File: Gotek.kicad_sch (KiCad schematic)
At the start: 72 parts, among them J10 Conn_01x04_Pin, J3 Conn_01x03_Pin, J4 Conn_01x02_Pin, J7 Display Port, P1 Conn_01x26, P3 USB_A, Q1 PMBT2222A,215, Q2 PMBT2222A,215, Q3 PMBT2222A,215, Q4 PMBT2222A,215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

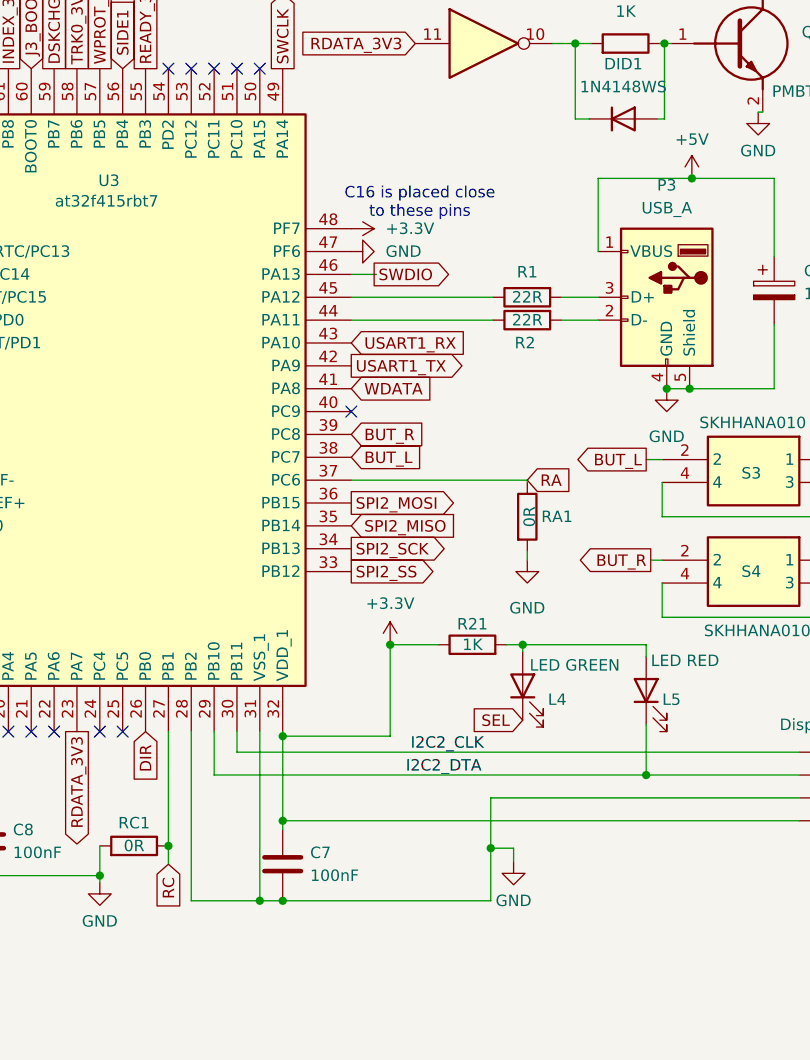
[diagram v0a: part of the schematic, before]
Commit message: Add files via upload
Updated to correct schematic positioning of C7 and C16. Layout did not change.
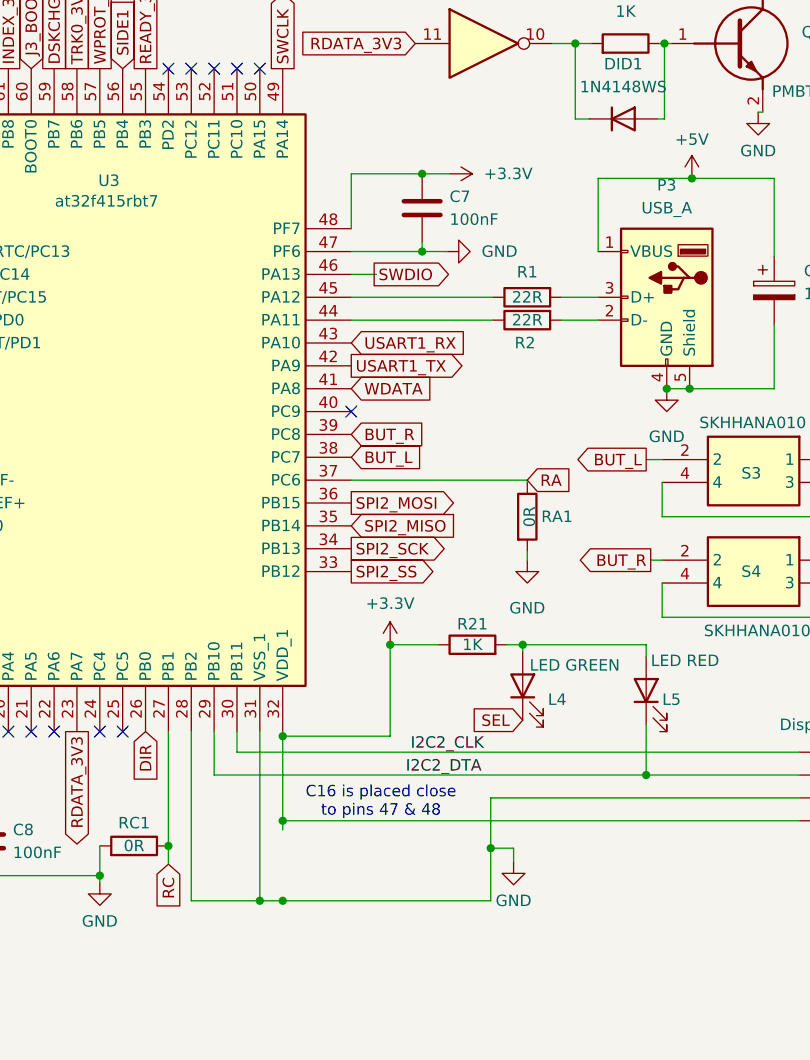
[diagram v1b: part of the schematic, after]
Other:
- note added: "C16 is placed close to pins 47 & 48"
- note removed: "C16 is placed close to these pins"
- moved on the sheet: C7
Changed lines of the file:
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@@
 	(title_block
 		(title "Gotek SFR1M44-DU26 (SFRC2D.B) Handrawn Schematic")
-		(date "2024-10-06")
+		(date "2024-10-09")
 		(rev "1.0")
 		(company "LiveBoxAndy")
 		(comment 1 "Based on pictures and meter readings.")
+		(comment 2 "Correct positions of C7 and C16 on schematic. Layout was correct")
 	)
 	(junction
@@
 	)
 	(junction
+		(at 231.394 92.456)
+		(diameter 0)
+		(color 0 0 0 0)
+	)
+	(junction
 		(at 280.416 33.274)
 		(diameter 0)
@@
 	)
 	(junction
+		(at 231.394 83.82)
+		(diameter 0)
+		(color 0 0 0 0)
+	)
+	(junction
 		(at 278.384 121.92)
 		(diameter 0)
@@
 	(wire
 		(pts
+			(xy 223.52 92.456) (xy 231.394 92.456)
+		)
+		(stroke
+			(width 0)
+			(type default)
+		)
+	)
+	(wire
+		(pts
 			(xy 227.838 136.144) (xy 233.172 136.144)
 		)
@@
 	(wire
 		(pts
+			(xy 231.394 92.456) (xy 234.188 92.456)
+		)
+		(stroke
+			(width 0)
+			(type default)
+		)
+	)
+	(wire
+		(pts
 			(xy 182.88 161.798) (xy 195.58 161.798)
 		)
@@
 	(wire
 		(pts
+			(xy 234.442 83.82) (xy 231.394 83.82)
+		)
+		(stroke
+			(width 0)
+			(type default)
+		)
+	)
+	(wire
+		(pts
 			(xy 258.572 107.696) (xy 261.112 107.696)
 		)
@@
 	(wire
 		(pts
+			(xy 223.52 83.82) (xy 231.394 83.82)
+		)
+		(stroke
+			(width 0)
+			(type default)
+		)
+	)
+	(wire
+		(pts
 			(xy 27.94 101.346) (xy 25.146 101.346)
 		)
@@
 	(wire
 		(pts
+			(xy 223.52 83.82) (xy 223.52 89.916)
+		)
+		(stroke
+			(width 0)
+			(type default)
+		)
+	)
+	(wire
+		(pts
 			(xy 60.706 41.148) (xy 106.426 41.148)
 		)
@@
 	(wire
 		(pts
+			(xy 231.394 91.44) (xy 231.394 92.456)
+		)
+		(stroke
+			(width 0)
+			(type default)
+		)
+	)
+	(wire
+		(pts
 			(xy 270.51 92.964) (xy 270.51 84.328)
 		)
@@
 		)
 	)
-	(text "C16 is placed close\nto these pins"
+	(text "C16 is placed close\nto pins 47 & 48"
 		(exclude_from_sim no)
-		(at 231.14 87.122 0)
+		(at 226.822 153.67 0)
 		(effects
 			(font
@@
 	(symbol
 		(lib_id "power:+3.3V")
-		(at 223.52 89.916 270)
+		(at 234.442 83.82 270)
 		(unit 1)
 		(exclude_from_sim no)
@@
 		(fields_autoplaced yes)
 		(property "Reference" "#PWR033"
-			(at 219.71 89.916 0)
+			(at 230.632 83.82 0)
 			(effects
 				(font
@@
 		)
 		(property "Value" "+3.3V"
-			(at 227.33 89.9159 90)
+			(at 238.252 83.8199 90)
 			(effects
 				(font
@@
 		)
 		(property "Footprint" ""
-			(at 223.52 89.916 0)
+			(at 234.442 83.82 0)
 			(effects
 				(font
@@
 		)
 		(property "Datasheet" ""
-			(at 223.52 89.916 0)
+			(at 234.442 83.82 0)
 			(effects
 				(font
@@
 		)
 		(property "Description" "Power symbol creates a global label with name \"+3.3V\""
-			(at 223.52 89.916 0)
+			(at 234.442 83.82 0)
 			(effects
 				(font
@@
 	(symbol
 		(lib_id "Device:C")
-		(at 215.9 160.528 0)
+		(at 231.394 87.63 0)
 		(unit 1)
 		(exclude_from_sim no)
@@
 		(fields_autoplaced yes)
 		(property "Reference" "C7"
-			(at 218.948 159.2579 0)
+			(at 234.442 86.3599 0)
 			(effects
 				(font
@@
 		)
 		(property "Value" "100nF"
-			(at 218.948 161.7979 0)
+			(at 234.442 88.8999 0)
 			(effects
 				(font
@@
 		)
 		(property "Footprint" "Capacitor_SMD:C_0805_2012Metric_Pad1.18x1.45mm_HandSolder"
-			(at 216.8652 164.338 0)
+			(at 232.3592 91.44 0)
 			(effects
 				(font
@@
 		)
 		(property "Datasheet" "~"
-			(at 215.9 160.528 0)
+			(at 231.394 87.63 0)
 			(effects
 				(font
@@
 		)
 		(property "Description" "Unpolarized capacitor"
-			(at 215.9 160.528 0)
+			(at 231.394 87.63 0)
 			(effects
 				(font
@@
 	(symbol
 		(lib_id "power:GND")
-		(at 223.52 92.456 90)
+		(at 234.188 92.456 90)
 		(unit 1)
 		(exclude_from_sim no)
@@
 		(fields_autoplaced yes)
 		(property "Reference" "#PWR032"
-			(at 229.87 92.456 0)
+			(at 240.538 92.456 0)
 			(effects
 				(font
@@
 		)
 		(property "Value" "GND"
-			(at 227.33 92.4559 90)
+			(at 237.998 92.4559 90)
 			(effects
 				(font
@@
 		)
 		(property "Footprint" ""
-			(at 223.52 92.456 0)
+			(at 234.188 92.456 0)
 			(effects
 				(font
@@
 		)
 		(property "Datasheet" ""
-			(at 223.52 92.456 0)
+			(at 234.188 92.456 0)
 			(effects
 				(font
@@
 		)
 		(property "Description" "Power symbol creates a global label with name \"GND\" , ground"
-			(at 223.52 92.456 0)
+			(at 234.188 92.456 0)
 			(effects
 				(font

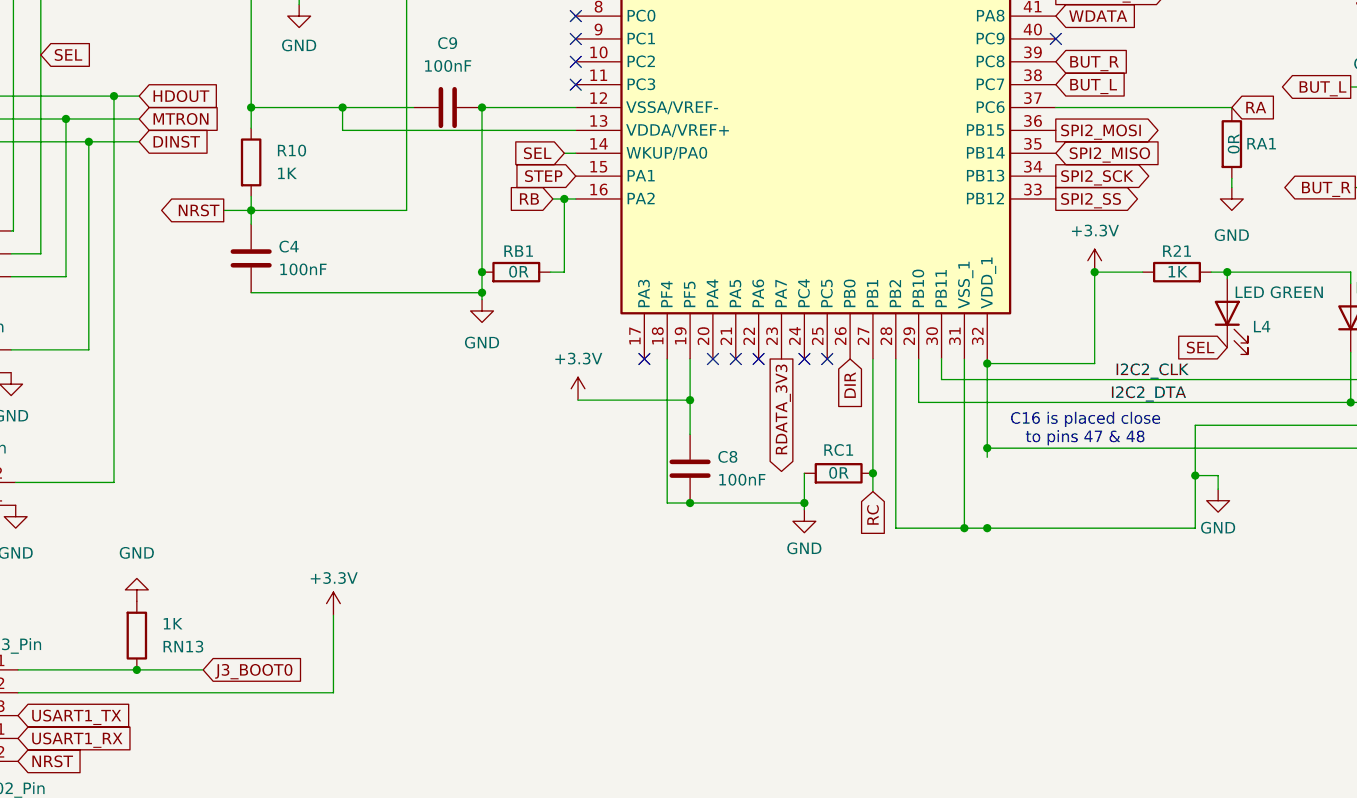
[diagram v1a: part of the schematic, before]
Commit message: Add files via upload
Corrected values for R10 and RN13 (4K7).
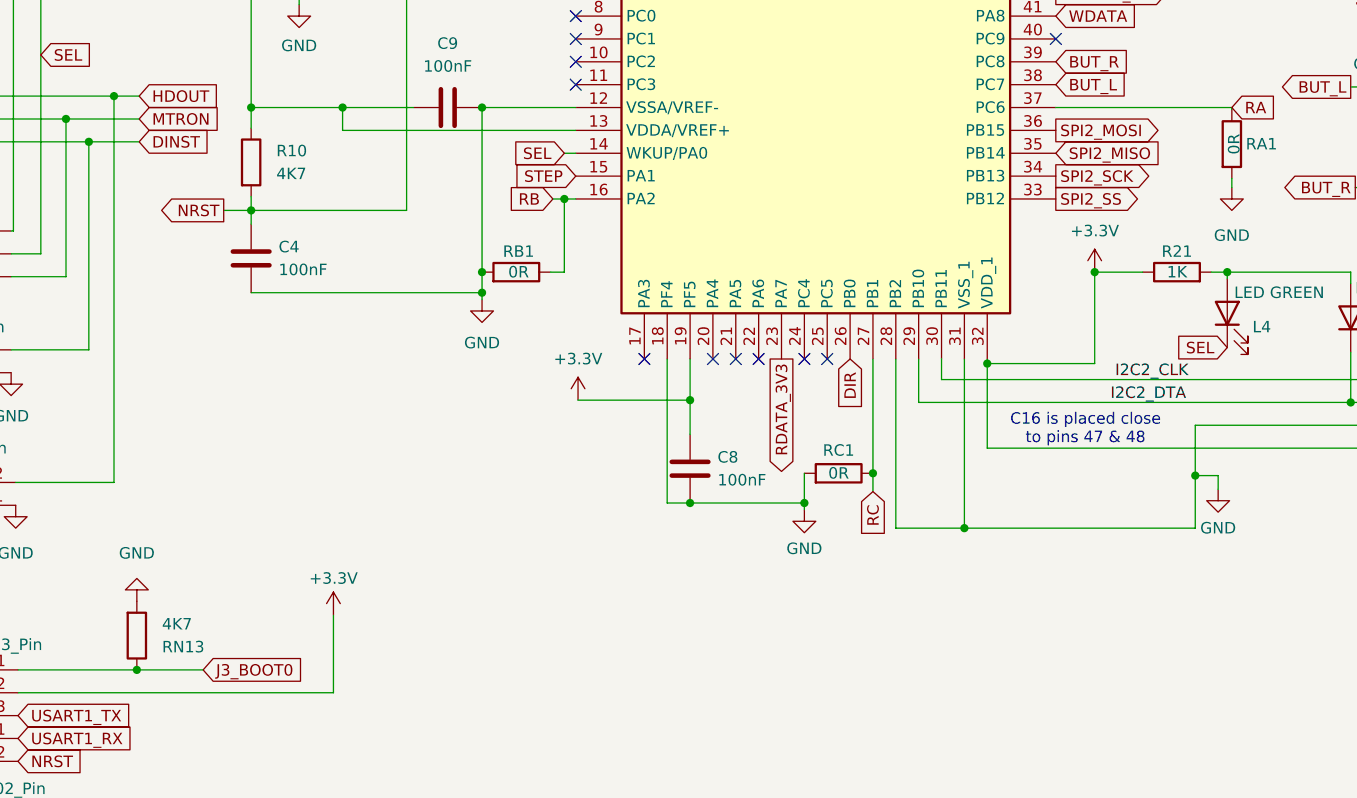
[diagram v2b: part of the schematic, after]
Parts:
- R10, RN13: value 1K -> 4K7
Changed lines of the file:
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@@
 	(title_block
 		(title "Gotek SFR1M44-DU26 (SFRC2D.B) Handrawn Schematic")
-		(date "2024-10-09")
+		(date "2024-10-10")
 		(rev "1.0")
 		(company "LiveBoxAndy")
 		(comment 1 "Based on pictures and meter readings.")
 		(comment 2 "Correct positions of C7 and C16 on schematic. Layout was correct")
+		(comment 3 "Correct values of R10 and RN13")
 	)
 	(junction
@@
 	)
 	(junction
-		(at 215.9 155.702)
-		(diameter 0)
-		(color 0 0 0 0)
-	)
-	(junction
 		(at 152.654 94.996)
 		(diameter 0)
@@
 	)
 	(junction
-		(at 215.9 164.592)
-		(diameter 0)
-		(color 0 0 0 0)
-	)
-	(junction
 		(at 227.838 136.144)
 		(diameter 0)
@@
 	(wire
 		(pts
-			(xy 215.9 164.592) (xy 213.36 164.592)
-		)
-		(stroke
-			(width 0)
-			(type default)
-		)
-	)
-	(wire
-		(pts
 			(xy 273.304 155.702) (xy 215.9 155.702)
 		)
@@
 	(wire
 		(pts
-			(xy 215.9 164.338) (xy 215.9 164.592)
-		)
-		(stroke
-			(width 0)
-			(type default)
-		)
-	)
-	(wire
-		(pts
 			(xy 65.786 25.654) (xy 115.57 25.654)
 		)
@@
 	(wire
 		(pts
-			(xy 239.014 164.592) (xy 215.9 164.592)
+			(xy 213.36 164.592) (xy 239.014 164.592)
 		)
 		(stroke
@@
 	(wire
 		(pts
-			(xy 215.9 155.702) (xy 215.9 156.718)
-		)
-		(stroke
-			(width 0)
-			(type default)
-		)
-	)
-	(wire
-		(pts
 			(xy 170.18 100.076) (xy 162.814 100.076)
 		)
@@
 			)
 		)
-		(property "Value" "1K"
+		(property "Value" "4K7"
 			(at 124.206 175.2601 0)
 			(effects
@@
 			)
 		)
-		(property "Value" "1K"
+		(property "Value" "4K7"
 			(at 136.906 125.2219 0)
 			(effects
